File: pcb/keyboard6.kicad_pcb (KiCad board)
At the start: 2 copper layers, 149.4 x 129.4 mm, 74 parts, among them J1 AudioJack4, J2 USB_B_Micro, SW0 SW_DIP_x01, SW1 SW_DIP_x01, SW10 SW_DIP_x01, SW11 SW_DIP_x01, SW12 SW_DIP_x01, SW13 SW_DIP_x01, SW14 SW_DIP_x01, SW15 SW_DIP_x01, SW16 SW_DIP_x01, SW17 SW_DIP_x01, SW18 SW_DIP_x01, SW19 SW_DIP_x01, SW2 SW_DIP_x01, SW20 SW_DIP_x01, SW21 SW_DIP_x01, SW22 SW_DIP_x01, SW23 SW_DIP_x01, SW24 SW_DIP_x01, SW25 SW_DIP_x01, SW26 SW_DIP_x01, SW27 SW_DIP_x01, SW28 SW_DIP_x01, SW29 SW_Push_Dual, SW3 SW_DIP_x01, SW4 SW_DIP_x01, SW5 SW_DIP_x01, SW6 SW_DIP_x01, SW7 SW_DIP_x01, SW8 SW_DIP_x01, SW9 SW_DIP_x01, Y1 16MHz

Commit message: Began with footprint placement script.
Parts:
- moved SW0 308.7 mm to (100.0, 100.0), turned to 90 degrees
- moved J2 261.9 mm to (-24.6, 9.90), turned to 270 degrees
- moved J1 239.1 mm to (-38.6, 9.10), turned to 270 degrees
- moved SW9 151.1 mm to (-42.3, -41.7)
- moved SW28 67.6 mm to (-59.0, -19.5)
- moved D25 41.7 mm to (-32.8, -4.19)
- moved D26 40.8 mm to (-34.1, -13.1)
- moved D27 38.6 mm to (-40.2, -0.63)

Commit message: Small changes to thumbs
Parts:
- SW1: renamed from SW22; footprint Button_Switch_Keyboard:SW_Cherry_MX_1.00u_PCB -> keyboard6:SW_Cherry_MX_1.00u_PCB_centered
- SW10: renamed from SW25; footprint Button_Switch_Keyboard:SW_Cherry_MX_1.00u_PCB -> keyboard6:SW_Cherry_MX_1.00u_PCB_centered
- SW11: renamed from SW20; footprint Button_Switch_Keyboard:SW_Cherry_MX_1.00u_PCB -> keyboard6:SW_Cherry_MX_1.00u_PCB_centered
- SW12: renamed from SW15; footprint Button_Switch_Keyboard:SW_Cherry_MX_1.00u_PCB -> keyboard6:SW_Cherry_MX_1.00u_PCB_centered
- SW13: renamed from SW9; footprint Button_Switch_Keyboard:SW_Cherry_MX_1.00u_PCB -> keyboard6:SW_Cherry_MX_1.00u_PCB_centered
- SW14: renamed from SW3; footprint Button_Switch_Keyboard:SW_Cherry_MX_1.00u_PCB -> keyboard6:SW_Cherry_MX_1.00u_PCB_centered
- SW15: renamed from SW24; footprint Button_Switch_Keyboard:SW_Cherry_MX_1.00u_PCB -> keyboard6:SW_Cherry_MX_1.00u_PCB_centered
- SW16: renamed from SW19; footprint Button_Switch_Keyboard:SW_Cherry_MX_1.00u_PCB -> keyboard6:SW_Cherry_MX_1.00u_PCB_centered
- SW17: renamed from SW14; footprint Button_Switch_Keyboard:SW_Cherry_MX_1.00u_PCB -> keyboard6:SW_Cherry_MX_1.00u_PCB_centered
- SW18: renamed from SW8; footprint Button_Switch_Keyboard:SW_Cherry_MX_1.00u_PCB -> keyboard6:SW_Cherry_MX_1.00u_PCB_centered
- SW19: renamed from SW2; footprint Button_Switch_Keyboard:SW_Cherry_MX_1.00u_PCB -> keyboard6:SW_Cherry_MX_1.00u_PCB_centered
- SW2: renamed from SW17; footprint Button_Switch_Keyboard:SW_Cherry_MX_1.00u_PCB -> keyboard6:SW_Cherry_MX_1.00u_PCB_centered
- SW20: renamed from SW18; footprint Button_Switch_Keyboard:SW_Cherry_MX_1.00u_PCB -> keyboard6:SW_Cherry_MX_1.00u_PCB_centered
- SW21: renamed from SW13; footprint Button_Switch_Keyboard:SW_Cherry_MX_1.00u_PCB -> keyboard6:SW_Cherry_MX_1.00u_PCB_centered
- SW22: renamed from SW7; footprint Button_Switch_Keyboard:SW_Cherry_MX_1.00u_PCB -> keyboard6:SW_Cherry_MX_1.00u_PCB_centered
- SW23: renamed from SW1; footprint Button_Switch_Keyboard:SW_Cherry_MX_1.00u_PCB -> keyboard6:SW_Cherry_MX_1.00u_PCB_centered
- SW24: renamed from SW12; footprint Button_Switch_Keyboard:SW_Cherry_MX_1.00u_PCB -> keyboard6:SW_Cherry_MX_1.00u_PCB_centered
- SW25: renamed from SW6; footprint Button_Switch_Keyboard:SW_Cherry_MX_1.00u_PCB -> keyboard6:SW_Cherry_MX_1.00u_PCB_centered
- SW26: renamed from SW0; footprint Button_Switch_Keyboard:SW_Cherry_MX_1.00u_PCB -> keyboard6:SW_Cherry_MX_1.00u_PCB_centered
- SW27: footprint Button_Switch_Keyboard:SW_Cherry_MX_1.00u_PCB -> keyboard6:SW_Cherry_MX_1.00u_PCB_centered
- SW28: renamed from SW23; footprint Button_Switch_Keyboard:SW_Cherry_MX_1.00u_PCB -> keyboard6:SW_Cherry_MX_1.00u_PCB_centered
- SW29: renamed from SW28; footprint Button_Switch_Keyboard:SW_Cherry_MX_1.00u_PCB -> keyboard6:SW_Cherry_MX_1.00u_PCB_centered
- SW3: renamed from SW11; footprint Button_Switch_Keyboard:SW_Cherry_MX_1.00u_PCB -> keyboard6:SW_Cherry_MX_1.00u_PCB_centered
- SW4: renamed from SW5; footprint Button_Switch_Keyboard:SW_Cherry_MX_1.00u_PCB -> keyboard6:SW_Cherry_MX_1.00u_PCB_centered
- SW5: renamed from SW26; footprint Button_Switch_Keyboard:SW_Cherry_MX_1.00u_PCB -> keyboard6:SW_Cherry_MX_1.00u_PCB_centered
- SW6: renamed from SW21; footprint Button_Switch_Keyboard:SW_Cherry_MX_1.00u_PCB -> keyboard6:SW_Cherry_MX_1.00u_PCB_centered
- SW7: renamed from SW16; footprint Button_Switch_Keyboard:SW_Cherry_MX_1.00u_PCB -> keyboard6:SW_Cherry_MX_1.00u_PCB_centered
- SW8: renamed from SW10; footprint Button_Switch_Keyboard:SW_Cherry_MX_1.00u_PCB -> keyboard6:SW_Cherry_MX_1.00u_PCB_centered
- SW9: renamed from SW4; footprint Button_Switch_Keyboard:SW_Cherry_MX_1.00u_PCB -> keyboard6:SW_Cherry_MX_1.00u_PCB_centered
- moved SW1 167.0 mm to (0.00, -19.1)
- moved SW4 148.8 mm to (0.00, -76.4)
- moved SW28 145.0 mm to (-20.7, 9.70), turned to 30.3 degrees
- moved SW14 91.0 mm to (38.2, -85.4)
- moved SW21 88.8 mm to (76.4, -23.1)
- moved SW24 84.2 mm to (95.5, -23.1)
- moved SW13 84.1 mm to (38.2, -66.3)
- moved SW17 76.2 mm to (57.3, -42.2)
- moved SW22 75.2 mm to (76.4, -42.2)
- moved SW26 69.8 mm to (95.5, 30.4), turned to 0 degrees
- moved SW18 69.6 mm to (57.3, -61.3)
- moved SW23 67.6 mm to (76.4, -61.3)
- moved SW5 58.0 mm to (19.1, -4.00)
- moved SW10 56.9 mm to (38.2, -9.00)
- moved SW25 54.3 mm to (95.5, -42.2)
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- renumbered D23 to D1, D26 to D10, D21 to D11, D16 to D12, D10 to D13, D4 to D14, D25 to D15, D20 to D16, D15 to D17, D9 to D18, D3 to D19, D18 to D2, D19 to D20, D14 to D21, D8 to D22, D2 to D23, D13 to D24, D7 to D25, D1 to D26, D28 to D27, D24 to D28, D12 to D3, D6 to D4, D27 to D5, D22 to D6, D17 to D7, D11 to D8, D5 to D9, SW29 to SW30

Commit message: Fix pcb clearance.
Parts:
- moved D11 115.8 mm to (-38.6, -9.10), turned to 270 degrees
- moved D10 9.99 mm to (-24.6, -9.90), turned to 270 degrees
- moved SW29 0.97 mm to (-38.0, 23.6), turned to 45.8 degrees
- moved SW28 0.82 mm to (-21.1, 10.4), turned to 30.4 degrees
- moved SW27 0.69 mm to (-1.35, 2.10)
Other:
- board size 149.4 x 129.4 mm -> 149.9 x 129.4 mm

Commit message: placed diodes in script.
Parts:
- moved C2 232.2 mm to (-0.35, 24.6)
- moved F1 221.8 mm to (14.3, 24.4)
- moved R2 218.1 mm to (14.6, 12.1), turned to 180 degrees
- moved C4 212.7 mm to (-7.21, 24.4)
- moved R3 210.6 mm to (14.7, 9.55), turned to 180 degrees
- moved C3 205.5 mm to (5.93, 24.5)
- moved C7 193.7 mm to (14.2, 20.6)
- moved mcu1 190.6 mm to (38.1, 12.3)
- moved C5 181.3 mm to (24.6, 24.1), turned to 180 degrees
- moved Y1 179.8 mm to (37.3, 24.1), turned to 180 degrees
- moved R1 174.5 mm to (65.3, 26.6)
- moved C6 170.9 mm to (35.3, 3.17), turned to 180 degrees
- moved C1 163.1 mm to (49.7, 24.1)
- moved SW30 156.7 mm to (70.0, 17.2)
- moved D19 106.1 mm to (53.3, -76.4)
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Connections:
- D1 pad 1: /Controller/col5 -> Net-(D1-Pad1)
- D1 pad 2: Net-(D1-Pad2) -> /Controller/col5
- D10 pad 1: /Controller/col3 -> Net-(D10-Pad1)
- D10 pad 2: Net-(D10-Pad2) -> /Controller/col3
- D11 pad 1: /Controller/col3 -> Net-(D11-Pad1)
- D11 pad 2: Net-(D11-Pad2) -> /Controller/col3
- D12 pad 1: /Controller/col3 -> Net-(D12-Pad1)
- D12 pad 2: Net-(D12-Pad2) -> /Controller/col3
- D13 pad 1: /Controller/col3 -> Net-(D13-Pad1)
- D13 pad 2: Net-(D13-Pad2) -> /Controller/col3
- D14 pad 1: /Controller/col3 -> Net-(D14-Pad1)
- D14 pad 2: Net-(D14-Pad2) -> /Controller/col3
- D15 pad 1: /Controller/col2 -> Net-(D15-Pad1)
- D15 pad 2: Net-(D15-Pad2) -> /Controller/col2
- D16 pad 1: /Controller/col2 -> Net-(D16-Pad1)
- D16 pad 2: Net-(D16-Pad2) -> /Controller/col2
- D17 pad 1: /Controller/col2 -> Net-(D17-Pad1)
- D17 pad 2: Net-(D17-Pad2) -> /Controller/col2
- D18 pad 1: /Controller/col2 -> Net-(D18-Pad1)
- D18 pad 2: Net-(D18-Pad2) -> /Controller/col2
- D19 pad 1: /Controller/col2 -> Net-(D19-Pad1)
- D19 pad 2: Net-(D19-Pad2) -> /Controller/col2
- D2 pad 1: /Controller/col5 -> Net-(D2-Pad1)
- D2 pad 2: Net-(D2-Pad2) -> /Controller/col5
- D20 pad 1: /Controller/col1 -> Net-(D20-Pad1)
- D20 pad 2: Net-(D20-Pad2) -> /Controller/col1
- D21 pad 1: /Controller/col1 -> Net-(D21-Pad1)
- D21 pad 2: Net-(D21-Pad2) -> /Controller/col1
- D22 pad 1: /Controller/col1 -> Net-(D22-Pad1)
- D22 pad 2: Net-(D22-Pad2) -> /Controller/col1
- D23 pad 1: /Controller/col1 -> Net-(D23-Pad1)
- D23 pad 2: Net-(D23-Pad2) -> /Controller/col1
- D24 pad 1: /Controller/col0 -> Net-(D24-Pad1)
- D24 pad 2: Net-(D24-Pad2) -> /Controller/col0
- D25 pad 1: /Controller/col0 -> Net-(D25-Pad1)
- D25 pad 2: Net-(D25-Pad2) -> /Controller/col0
- D26 pad 1: /Controller/col0 -> Net-(D26-Pad1)
- D26 pad 2: Net-(D26-Pad2) -> /Controller/col0
- D27 pad 1: /Controller/col5 -> Net-(D27-Pad1)
- D27 pad 2: Net-(D27-Pad2) -> /Controller/col5
- D28 pad 1: /Controller/col0 -> Net-(D28-Pad1)
- D28 pad 2: Net-(D28-Pad2) -> /Controller/col0
- D29 pad 1: /Controller/col0 -> Net-(D29-Pad1)
- D29 pad 2: Net-(D29-Pad2) -> /Controller/col0
- D3 pad 1: /Controller/col5 -> Net-(D3-Pad1)
- D3 pad 2: Net-(D3-Pad2) -> /Controller/col5
- D4 pad 1: /Controller/col5 -> Net-(D4-Pad1)
- D4 pad 2: Net-(D4-Pad2) -> /Controller/col5
- D5 pad 1: /Controller/col4 -> Net-(D5-Pad1)
- D5 pad 2: Net-(D5-Pad2) -> /Controller/col4
- D6 pad 1: /Controller/col4 -> Net-(D6-Pad1)
- D6 pad 2: Net-(D6-Pad2) -> /Controller/col4
- D7 pad 1: /Controller/col4 -> Net-(D7-Pad1)
- D7 pad 2: Net-(D7-Pad2) -> /Controller/col4
- D8 pad 1: /Controller/col4 -> Net-(D8-Pad1)
- D8 pad 2: Net-(D8-Pad2) -> /Controller/col4
- D9 pad 1: /Controller/col4 -> Net-(D9-Pad1)
- D9 pad 2: Net-(D9-Pad2) -> /Controller/col4
- SW1 pad 2: Net-(D1-Pad2) -> Net-(D1-Pad1)
- SW10 pad 2: Net-(D10-Pad2) -> Net-(D10-Pad1)
- SW11 pad 2: Net-(D11-Pad2) -> Net-(D11-Pad1)
- SW12 pad 2: Net-(D12-Pad2) -> Net-(D12-Pad1)
- SW13 pad 2: Net-(D13-Pad2) -> Net-(D13-Pad1)
- SW14 pad 2: Net-(D14-Pad2) -> Net-(D14-Pad1)
- SW15 pad 2: Net-(D15-Pad2) -> Net-(D15-Pad1)
- SW16 pad 2: Net-(D16-Pad2) -> Net-(D16-Pad1)
- SW17 pad 2: Net-(D17-Pad2) -> Net-(D17-Pad1)
- SW18 pad 2: Net-(D18-Pad2) -> Net-(D18-Pad1)
- SW19 pad 2: Net-(D19-Pad2) -> Net-(D19-Pad1)
- SW2 pad 2: Net-(D2-Pad2) -> Net-(D2-Pad1)
- SW20 pad 2: Net-(D20-Pad2) -> Net-(D20-Pad1)
- SW21 pad 2: Net-(D21-Pad2) -> Net-(D21-Pad1)
- SW22 pad 2: Net-(D22-Pad2) -> Net-(D22-Pad1)
- SW23 pad 2: Net-(D23-Pad2) -> Net-(D23-Pad1)
- SW24 pad 2: Net-(D24-Pad2) -> Net-(D24-Pad1)
- SW25 pad 2: Net-(D25-Pad2) -> Net-(D25-Pad1)
- SW26 pad 2: Net-(D26-Pad2) -> Net-(D26-Pad1)
- SW27 pad 2: Net-(D27-Pad2) -> Net-(D27-Pad1)
- SW28 pad 2: Net-(D28-Pad2) -> Net-(D28-Pad1)
- SW29 pad 2: Net-(D29-Pad2) -> Net-(D29-Pad1)
- SW3 pad 2: Net-(D3-Pad2) -> Net-(D3-Pad1)
- SW4 pad 2: Net-(D4-Pad2) -> Net-(D4-Pad1)
- SW5 pad 2: Net-(D5-Pad2) -> Net-(D5-Pad1)
- SW6 pad 2: Net-(D6-Pad2) -> Net-(D6-Pad1)
- SW7 pad 2: Net-(D7-Pad2) -> Net-(D7-Pad1)
- SW8 pad 2: Net-(D8-Pad2) -> Net-(D8-Pad1)
- SW9 pad 2: Net-(D9-Pad2) -> Net-(D9-Pad1)
- mcu1 pad 1: /Controller/col5 -> Net-(mcu1-Pad1)
- mcu1 pad 12: /Controller/col2 -> Net-(mcu1-Pad12)
- mcu1 pad 26: /Controller/col1 -> Net-(mcu1-Pad26)
- mcu1 pad 27: Net-(mcu1-Pad27) -> /Controller/col0
- mcu1 pad 28: Net-(mcu1-Pad28) -> /Controller/col1
- mcu1 pad 29: /Controller/col4 -> /Controller/col2
- mcu1 pad 31: Net-(mcu1-Pad31) -> /Controller/col4
- mcu1 pad 32: /Controller/col0 -> /Controller/col5
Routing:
- net /Controller/col5: track 0.00 -> 63.9 mm
- net (no net): track 0.00 -> 58.4 mm
- net Net-(J2-Pad3): track 0.00 -> 45.7 mm
- net Net-(J2-Pad2): track 0.00 -> 43.2 mm
- net Net-(R2-Pad1): track 0.00 -> 17.4 mm
- net Net-(R3-Pad1): track 0.00 -> 16.8 mm

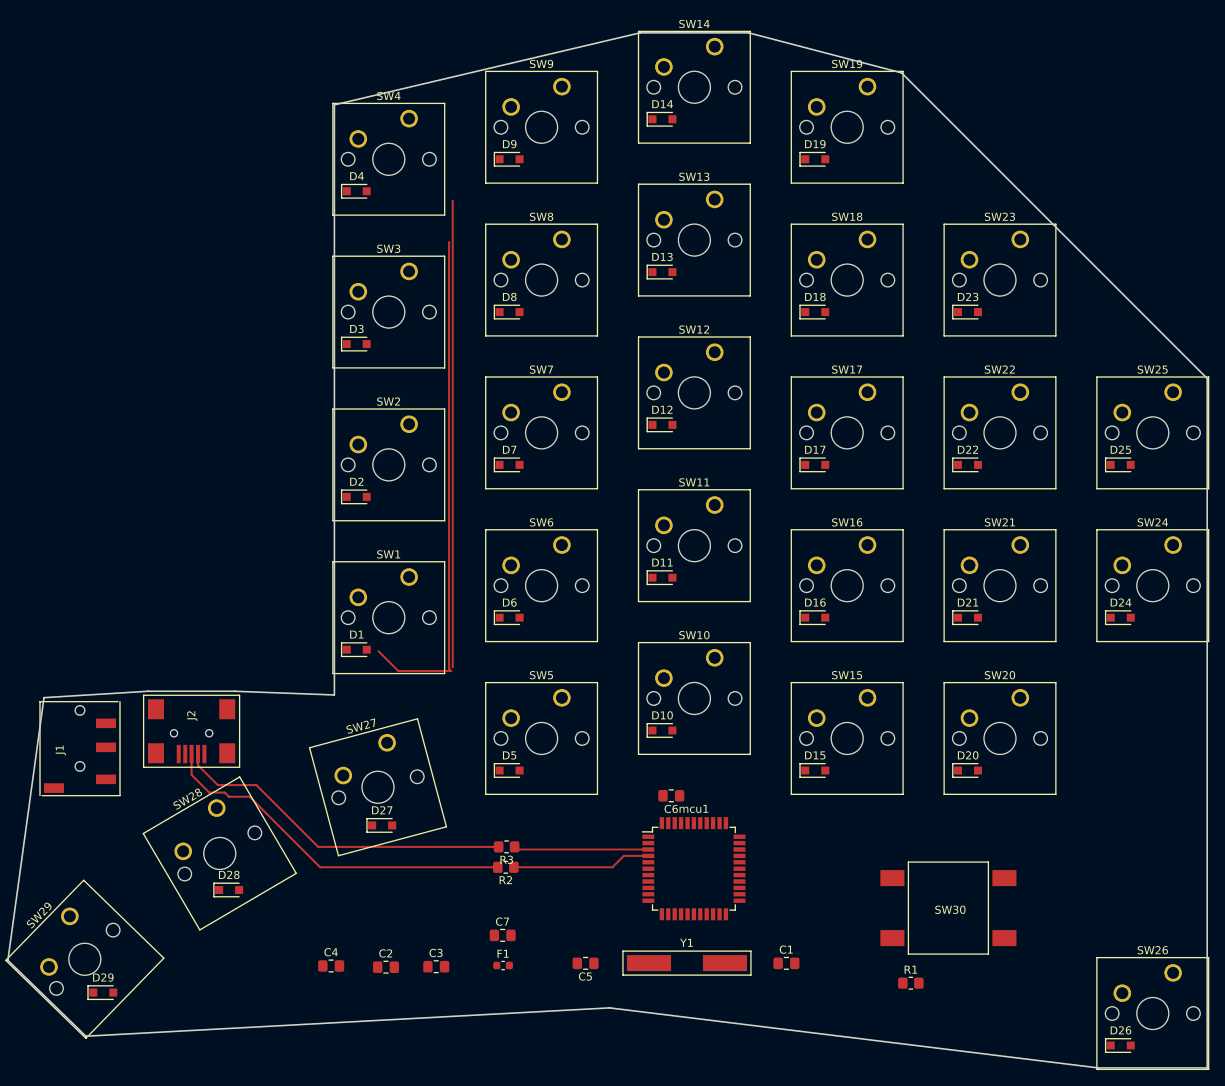
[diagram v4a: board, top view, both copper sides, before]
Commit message: Switches routed.
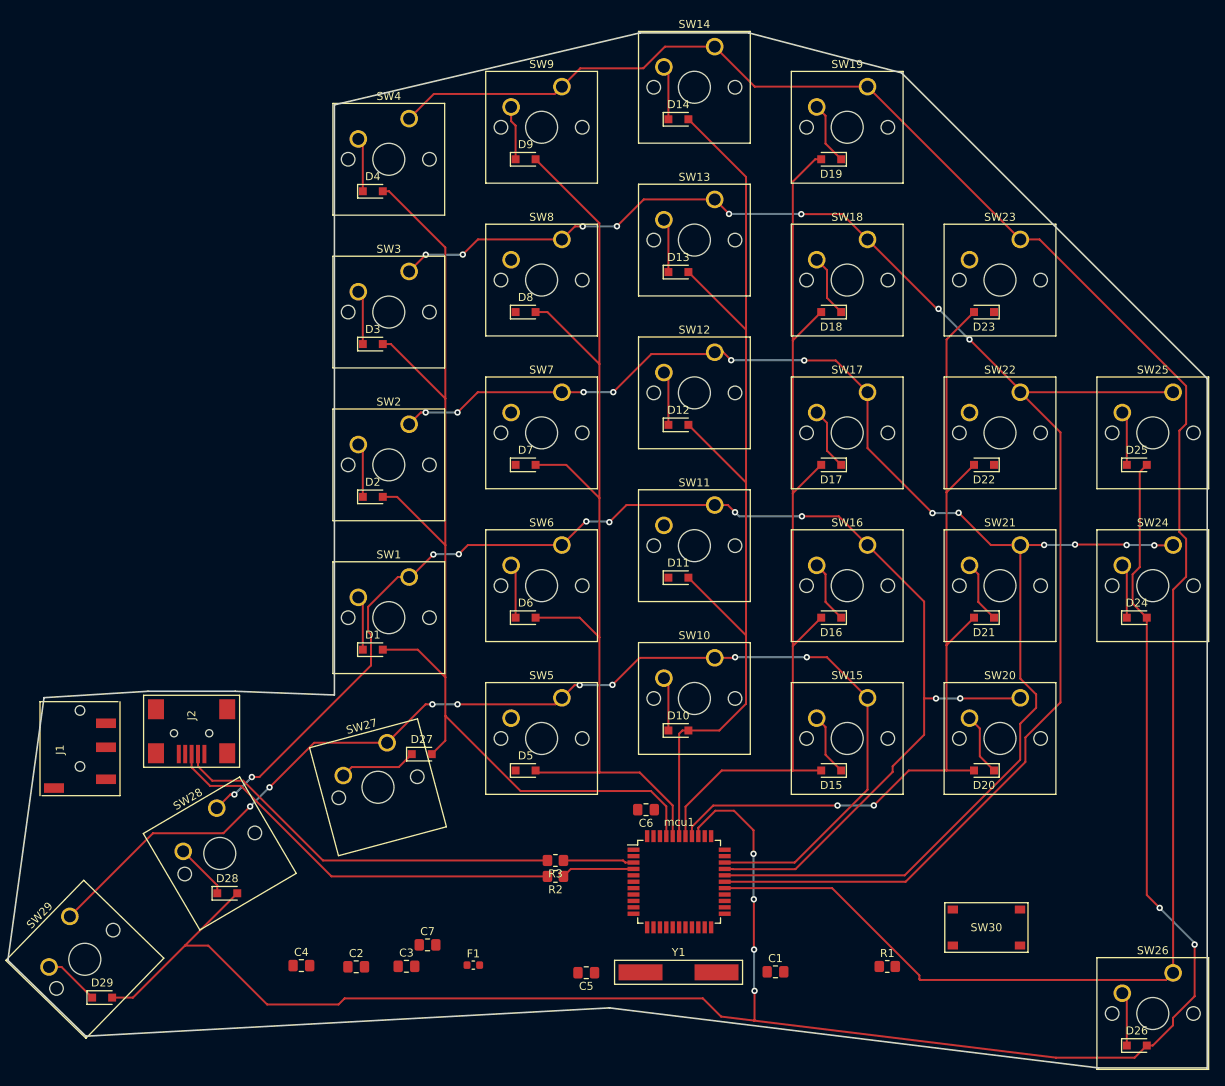
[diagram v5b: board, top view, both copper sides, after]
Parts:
- SW30: footprint keyboard6:schurter sms gullwing lead -> keyboard6:C_K_PTS641SP31SMTR2LFS
- moved D27 10.2 mm to (4.12, -2.04)
- moved C7 9.47 mm to (4.84, 21.8)
- moved R3 6.33 mm to (20.8, 11.2)
- moved R2 6.30 mm to (20.8, 13.2)
- moved SW30 5.34 mm to (74.7, 19.6)
- moved C4 3.72 mm to (-10.9, 24.4)
- moved C3 3.72 mm to (2.21, 24.5)
- moved C2 3.72 mm to (-4.07, 24.5)
- moved F1 3.72 mm to (10.6, 24.3)
- moved R1 3.62 mm to (62.3, 24.5)
- moved C6 3.60 mm to (32.2, 4.90)
- moved mcu1 2.47 mm to (36.3, 13.9)
- moved D5 2.00 mm to (17.1, 0.00)
- moved D6 2.00 mm to (17.1, -19.1)
- moved D7 2.00 mm to (17.1, -38.2)
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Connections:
- mcu1 pad 27: /Controller/col0 -> /Controller/row0
- mcu1 pad 28: /Controller/col1 -> /Controller/row1
- mcu1 pad 29: /Controller/col2 -> /Controller/row2
- mcu1 pad 30: /Controller/col3 -> /Controller/row3
- mcu1 pad 31: /Controller/col4 -> /Controller/row4
- mcu1 pad 32: /Controller/col5 -> Net-(mcu1-Pad32)
- mcu1 pad 36: /Controller/row0 -> /Controller/col0
- mcu1 pad 37: /Controller/row1 -> /Controller/col1
- mcu1 pad 38: /Controller/row2 -> /Controller/col2
- mcu1 pad 39: /Controller/row3 -> /Controller/col3
- mcu1 pad 40: /Controller/row4 -> /Controller/col4
- mcu1 pad 41: Net-(mcu1-Pad41) -> /Controller/col5
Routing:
- net /Controller/col0: track 0.00 -> 259.7 mm, vias 0 -> 6
- net /Controller/row0: track 0.00 -> 254.6 mm
- net /Controller/row1: track 0.00 -> 203.3 mm, vias 0 -> 8
- net /Controller/row2: track 0.00 -> 184.8 mm, vias 0 -> 12
- net /Controller/row3: track 0.00 -> 175.0 mm, vias 0 -> 10
- net /Controller/row4: track 0.00 -> 148.3 mm, vias 0 -> 8
- net /Controller/col4: track 0.00 -> 132.1 mm
- net /Controller/col3: track 0.00 -> 129.3 mm
- net /Controller/col2: track 0.00 -> 115.9 mm
- net /Controller/col1: track 0.00 -> 107.8 mm, vias 0 -> 2
- net /Controller/col5: track 63.9 -> 141.0 mm
- net (no net): track 58.4 -> 0.00 mm
- net Net-(D27-Pad1): track 0.00 -> 9.66 mm
- net Net-(R2-Pad1): track 17.4 -> 9.15 mm
- net Net-(R3-Pad1): track 16.8 -> 8.87 mm
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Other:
- net class Default: clearance 0.2 -> 0.4
- rule trace_clearance: 0.2 -> 0.4
